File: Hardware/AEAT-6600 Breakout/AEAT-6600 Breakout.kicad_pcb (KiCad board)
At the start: 2 copper layers, 42.3 x 42.3 mm, 26 parts, among them J1 Conn_01x07, J2 Conn_01x09, U1 AEAT-6600-T16

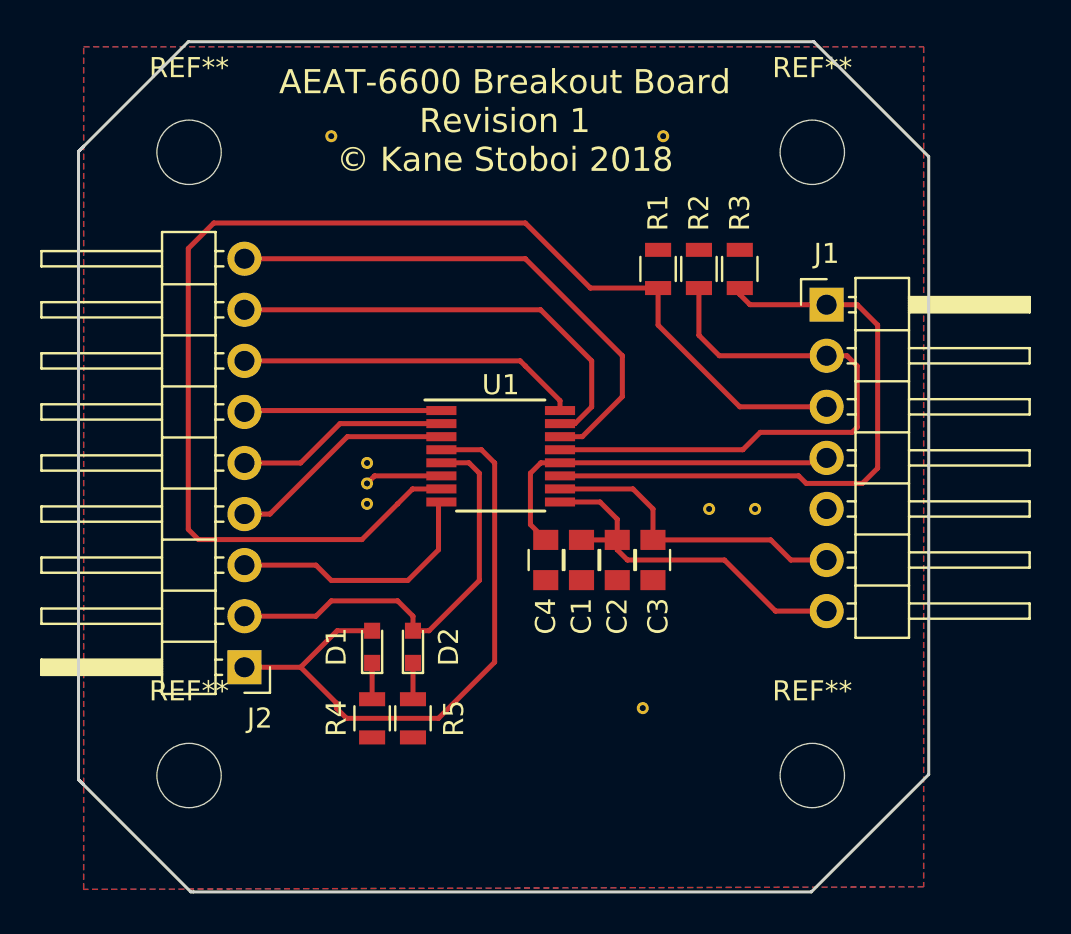
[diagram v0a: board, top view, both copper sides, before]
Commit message: Completed breakout boards and BOM
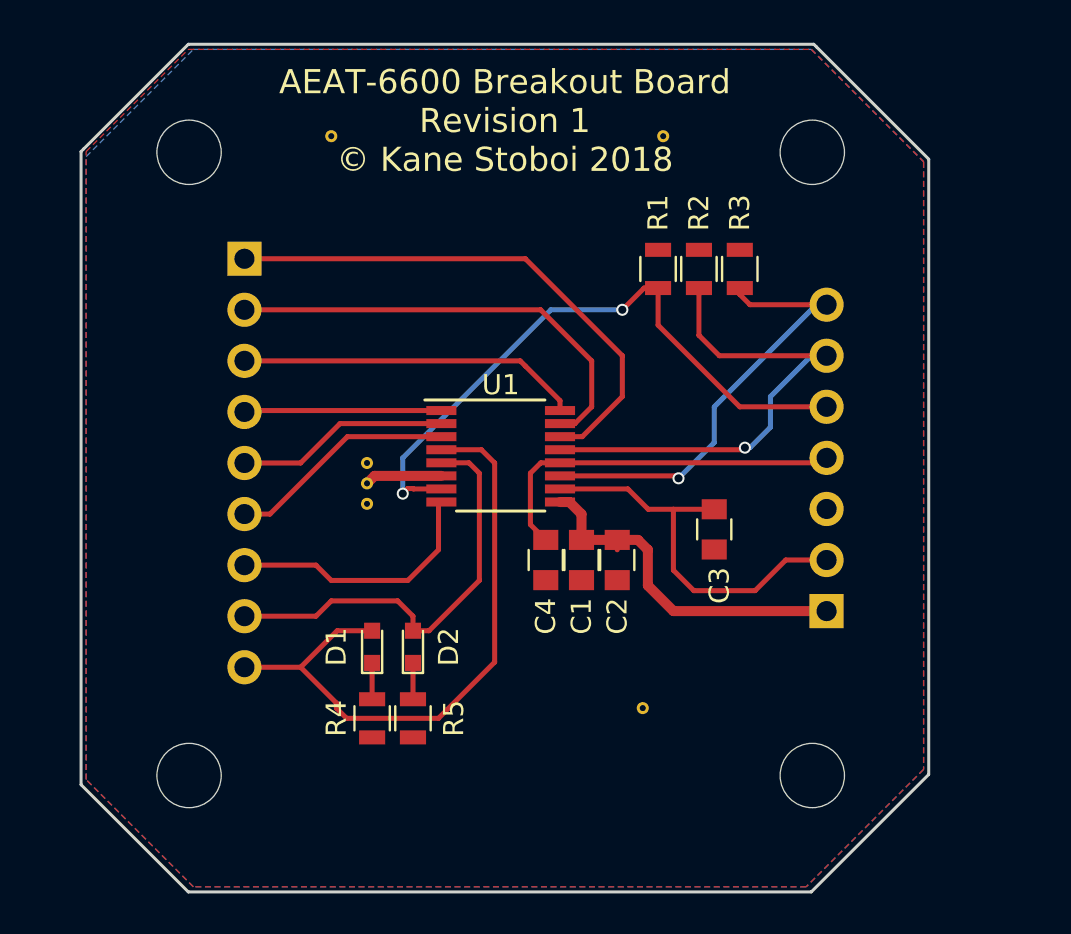
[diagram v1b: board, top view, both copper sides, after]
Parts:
- ? (x4): renamed from REF**; value MountingHole_3.2mm_M3 -> (none)
- J1, J2: moved to B.Cu
- R3: value 47 -> 47k
- moved J2 20.3 mm to (128.3, 105.9)
- moved J1 15.2 mm to (157.2, 123.4)
- moved C3 3.41 mm to (151.6, 119.4)
- moved REF** 3.06 mm to (154.4, 118.6)
- moved REF** 0.92 mm to (152.9, 117.9)
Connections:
- J1 pad 1: PWRDOWN -> 5V
- J1 pad 2: PROG -> VDD_F
- J1 pad 3: ALIGN -> GND
- J1 pad 5: GND -> ALIGN
- J1 pad 6: VDD_F -> PROG
- J1 pad 7: 5V -> PWRDOWN
- J2 pad 1: MAGHI -> NCS
- J2 pad 2: MAGLO -> CLK
- J2 pad 3: PWM -> DO/DI
- J2 pad 4: I/W -> A/U
- J2 pad 6: A/U -> I/W
- J2 pad 7: DO/DI -> PWM
- J2 pad 8: CLK -> MAGLO
- J2 pad 9: NCS -> MAGHI
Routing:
- net ALIGN: track 65.0 -> 31.9 mm, vias 0 -> 2
- net PWRDOWN: track 31.2 -> 22.8 mm, vias 0 -> 1
- net VDD_F: track 15.6 -> 19.8 mm
- net PROG: track 29.2 -> 25.2 mm, vias 0 -> 1
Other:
- board size 42.3 x 42.3 mm -> 42.2 x 42.2 mm
- net class POWER added: clearance 0.1, trace_width 0.5, via_dia 0.6, via_drill 0.4
- board text added: "5V"
- board text added: "6.5V"
- board text added: "A/U"
- board text added: "ALIGN"
- board text added: "B/V"
- board text added: "CLK"
- board text added: "DI"
- board text added: "GND"
- board text added: "I/W"
- board text added: "MAGHI"
- board text added: "MAGLO"
- board text added: "NCS"
- board text added: "PROG"
- board text added: "PWM"
- board text added: "PWRDOWN"
- board text added: "VDD F"
